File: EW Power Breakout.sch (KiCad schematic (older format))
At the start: 15 parts, among them J1 CONN_02X08, J2 JACK_2P, J3 JACK_2P, J4 JACK_2P, J5 JACK_2P, J6 CONN_01X14, U1 LM7805

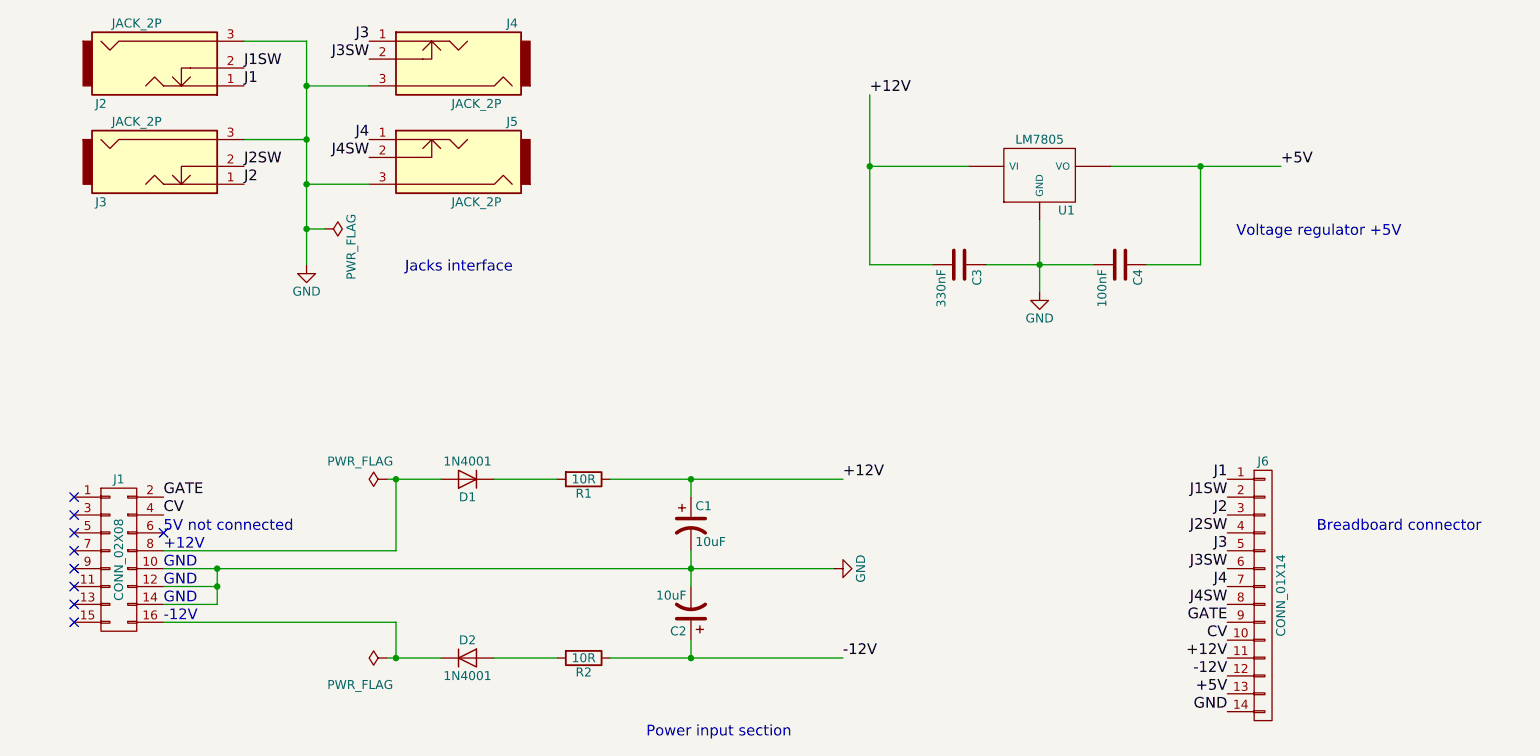
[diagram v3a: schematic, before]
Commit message: Fixed IDC routing bug
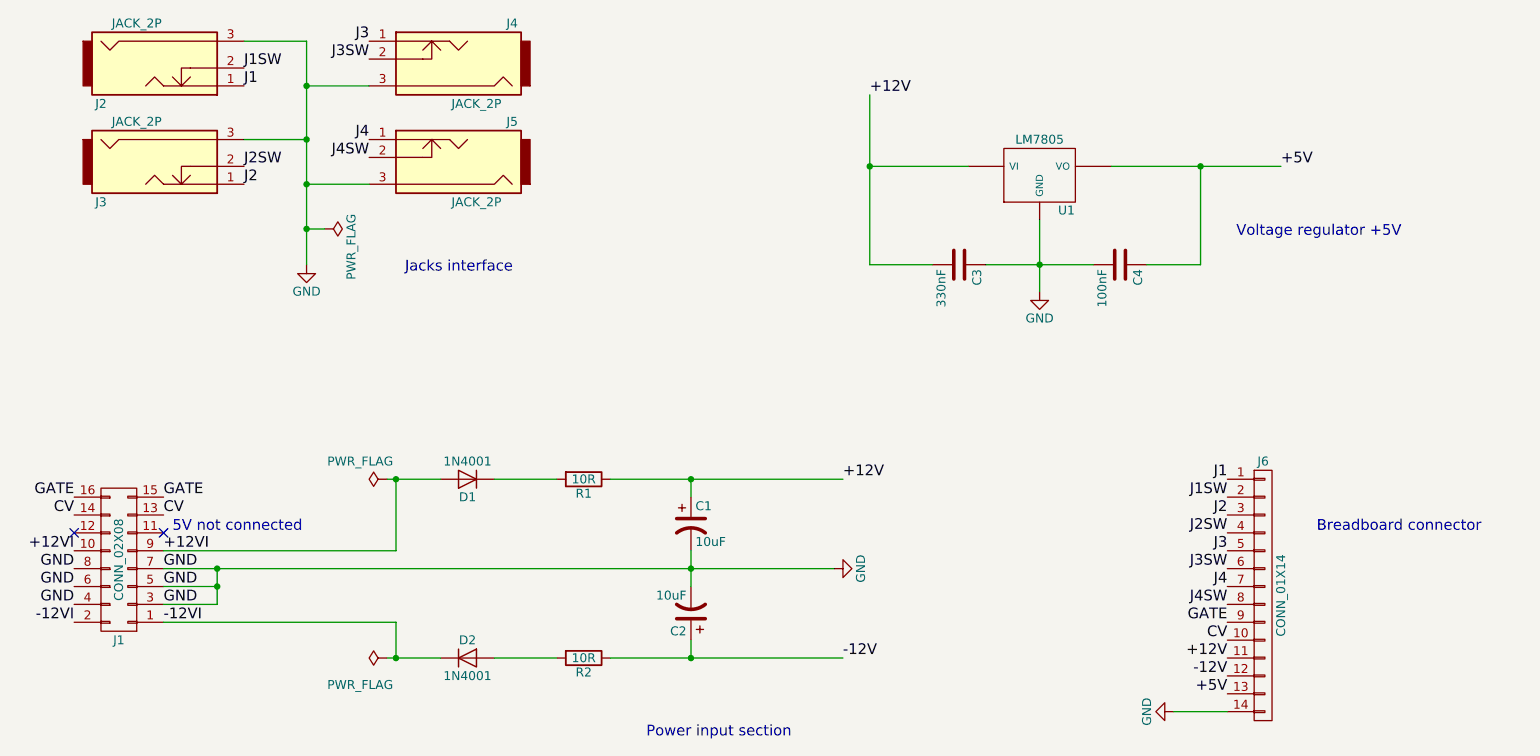
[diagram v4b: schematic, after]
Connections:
- net CV: now also J1.13 (P13), J1.14 (P14); no longer J1.4 (P4)
- net GATE: now also J1.15 (P15), J1.16 (P16); no longer J1.2 (P2)
- net GND: now also J1.3 (P3), J1.4 (P4), J1.5 (P5), J1.6 (P6), J1.7 (P7), J1.8 (P8); no longer J1.10 (P10), J1.12 (P12), J1.14 (P14)
- net -12VI: now reaches J1.1 (P1)
- net -12VI: now also D2.1 (K), J1.2 (P2)
- net +12VI: now reaches D1.2 (A)
- net +12VI: now also J1.10 (P10), J1.9 (P9); no longer J1.8 (P8)
- no-connect marks 9 -> 2
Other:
- note removed: "+12V"
- note removed: "-12V"
- note removed: "GND"
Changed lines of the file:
@@
 F 3 "" H 1900 2750 50  0001 C CNN
 	1    1900 3950
-	1    0    0    -1
+	-1   0    0    1
 $EndComp
 $Comp
@@
 Text Label 8100 4700 2    60   ~ 0
 +5V
-Text Label 8100 4800 2    60   ~ 0
-GND
 Text Label 2600 1850 0    60   ~ 0
 J2
@@
 CV
 NoConn ~ 2150 3800
-Text Notes 2150 3800 0    60   ~ 0
+Text Notes 2200 3800 0    60   ~ 0
 5V not connected
-Text Notes 2150 3900 0    60   ~ 0
-+12V
-Text Notes 2150 4000 0    60   ~ 0
-GND
-Text Notes 2150 4100 0    60   ~ 0
-GND
-Text Notes 2150 4200 0    60   ~ 0
-GND
-Text Notes 2150 4300 0    60   ~ 0
--12V
 $Comp
 L D D1
@@
 Text Label 6100 1350 0    60   ~ 0
 +12V
-NoConn ~ 1650 3600
-NoConn ~ 1650 3700
-NoConn ~ 1650 3800
-NoConn ~ 1650 3900
-NoConn ~ 1650 4000
-NoConn ~ 1650 4100
-NoConn ~ 1650 4200
-NoConn ~ 1650 4300
 Wire Wire Line
 	3050 2100 2950 2100
@@
 Text Notes 4850 4950 0    60   ~ 0
 Power input section
+Text Label 1650 3600 2    60   ~ 0
+GATE
+Text Label 1650 3700 2    60   ~ 0
+CV
+NoConn ~ 1650 3800
+Text Label 2150 4000 0    60   ~ 0
+GND
+Text Label 2150 4100 0    60   ~ 0
+GND
+Text Label 2150 4200 0    60   ~ 0
+GND
+Text Label 1650 4000 2    60   ~ 0
+GND
+Text Label 1650 4100 2    60   ~ 0
+GND
+Text Label 1650 4200 2    60   ~ 0
+GND
+Text Label 2150 3900 0    60   ~ 0
++12VI
+Text Label 1650 3900 2    60   ~ 0
++12VI
+Text Label 2150 4300 0    60   ~ 0
+-12VI
+Text Label 1650 4300 2    60   ~ 0
+-12VI
+$Comp
+L GND #PWR?
+U 1 1 599F1279
+P 7800 4800
+F 0 "#PWR?" H 7800 4550 50  0001 C CNN
+F 1 "GND" H 7800 4650 50  0000 C CNN
+F 2 "" H 7800 4800 50  0001 C CNN
+F 3 "" H 7800 4800 50  0001 C CNN
+	1    7800 4800
+	0    1    1    0
+$EndComp
+Wire Wire Line
+	7800 4800 8100 4800
 $EndSCHEMATC

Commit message: Drills in PJ301M-12 jacks
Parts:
- J2, J3, J4, J5: footprint Eurocad:PJ301M-12 -> lib:PJ301M-12
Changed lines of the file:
@@
 F 0 "J2" H 1800 1000 50  0000 C CNN
 F 1 "JACK_2P" H 2000 1450 50  0000 C CNN
-F 2 "Eurocad:PJ301M-12" H 2150 1200 50  0001 C CNN
+F 2 "lib:PJ301M-12" H 2150 1200 50  0001 C CNN
 F 3 "" H 2150 1200 50  0001 C CNN
 	1    2150 1200
@@
 F 0 "J3" H 1800 1550 50  0000 C CNN
 F 1 "JACK_2P" H 2000 2000 50  0000 C CNN
-F 2 "Eurocad:PJ301M-12" H 2150 1750 50  0001 C CNN
+F 2 "lib:PJ301M-12" H 2150 1750 50  0001 C CNN
 F 3 "" H 2150 1750 50  0001 C CNN
 	1    2150 1750
@@
 F 0 "J4" H 3400 950 50  0000 C CNN
 F 1 "JACK_2P" H 3600 1400 50  0000 C CNN
-F 2 "Eurocad:PJ301M-12" H 3750 1150 50  0001 C CNN
+F 2 "lib:PJ301M-12" H 3750 1150 50  0001 C CNN
 F 3 "" H 3750 1150 50  0001 C CNN
 	1    3750 1150
@@
 F 0 "J5" H 3400 1500 50  0000 C CNN
 F 1 "JACK_2P" H 3600 1950 50  0000 C CNN
-F 2 "Eurocad:PJ301M-12" H 3750 1700 50  0001 C CNN
+F 2 "lib:PJ301M-12" H 3750 1700 50  0001 C CNN
 F 3 "" H 3750 1700 50  0001 C CNN
 	1    3750 1700
@@
 	2950 1600 2600 1600
 Wire Wire Line
-	5900 4000 2150 4000
+	2150 4000 5900 4000
 Wire Wire Line
 	4000 4500 4350 4500
@@
 +12V
 Wire Wire Line
-	6100 2300 6100 1350
+	6100 1350 6100 2300
 Wire Wire Line
 	6650 1750 6100 1750
@@
 Connection ~ 7050 2300
 Wire Wire Line
-	6450 2300 6100 2300
+	6100 2300 6450 2300
 Text Notes 8600 3800 0    60   ~ 0
 Breadboard connector
@@
 -12VI
 $Comp
-L GND #PWR?
+L GND #PWR07
 U 1 1 599F1279
 P 7800 4800
-F 0 "#PWR?" H 7800 4550 50  0001 C CNN
+F 0 "#PWR07" H 7800 4550 50  0001 C CNN
 F 1 "GND" H 7800 4650 50  0000 C CNN
 F 2 "" H 7800 4800 50  0001 C CNN

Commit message: Wiring PCB
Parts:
- J2, J3, J4, J5: symbol JACK_2P -> JACK_2P-RESCUE-EW_Power_Breakout
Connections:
- net GND: now also J2.1, J3.1, J4.1, J5.1; no longer J2.3, J3.3, J4.3, J5.3
- net J1: now also J2.3; no longer J2.1
- net J2: now also J3.3; no longer J3.1
- net J3: now also J4.3; no longer J4.1
- net J4: now also J5.3; no longer J5.1
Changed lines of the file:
@@
 EESchema Schematic File Version 2
+LIBS:EW Power Breakout-rescue
 LIBS:power
 LIBS:device
@@
 $EndComp
 $Comp
-L JACK_2P J2
+L JACK_2P-RESCUE-EW_Power_Breakout J2
 U 1 1 599C45B8
 P 2150 1200
@@
 $EndComp
 $Comp
-L JACK_2P J3
+L JACK_2P-RESCUE-EW_Power_Breakout J3
 U 1 1 599C461E
 P 2150 1750
@@
 $EndComp
 $Comp
-L JACK_2P J4
+L JACK_2P-RESCUE-EW_Power_Breakout J4
 U 1 1 599C4645
 P 3750 1150
@@
 $EndComp
 $Comp
-L JACK_2P J5
+L JACK_2P-RESCUE-EW_Power_Breakout J5
 U 1 1 599C4690
 P 3750 1700
